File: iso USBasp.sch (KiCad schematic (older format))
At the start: 103 parts

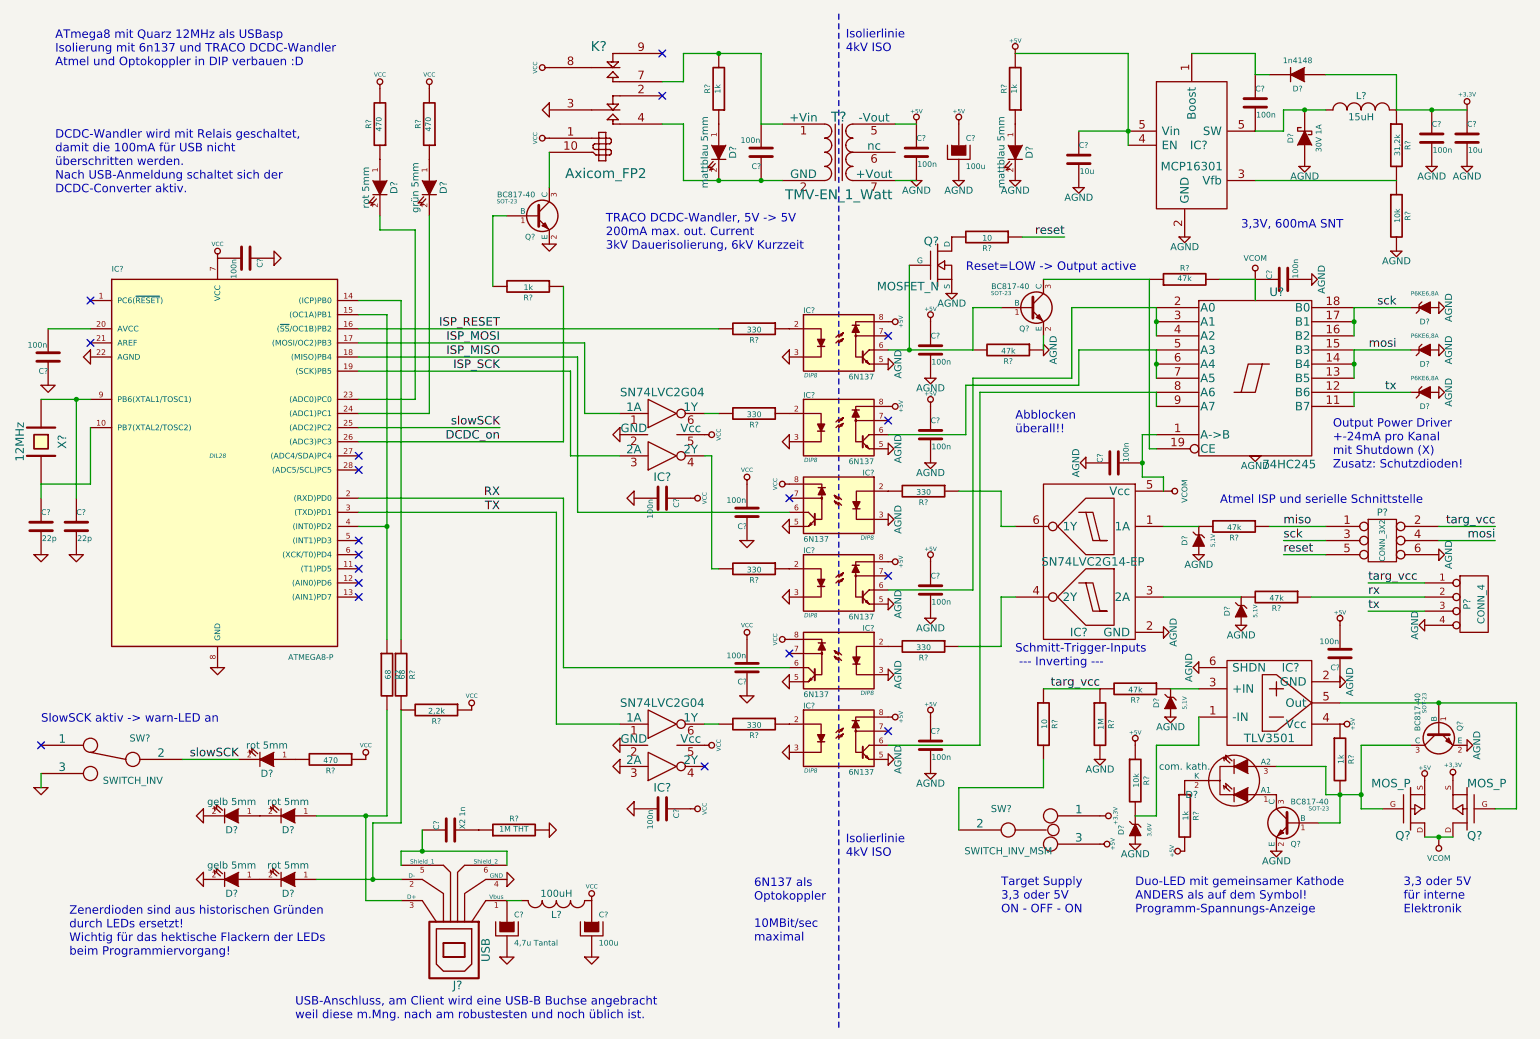
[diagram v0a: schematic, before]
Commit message: zuordunugsdateien schaltplan -> footprints dazu, aber noch nicht fertig. + noch ein paar Änderungen am Schaltplan
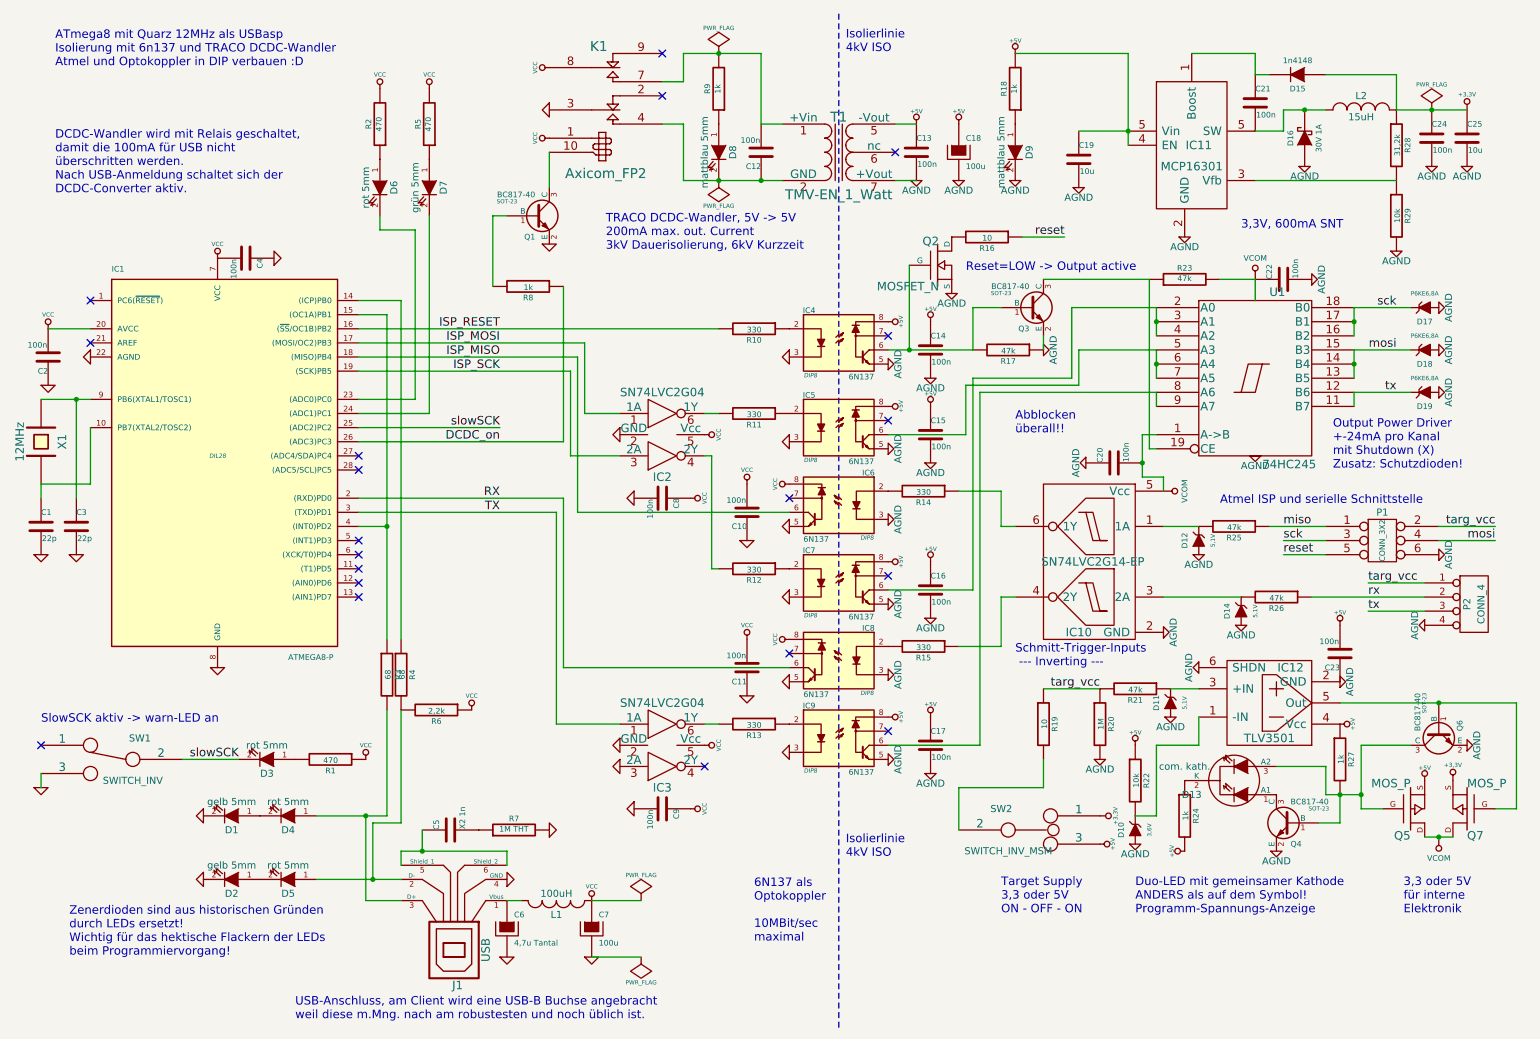
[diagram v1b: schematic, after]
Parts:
- gave numbers to parts that had none: 103
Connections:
- net VCC: now also C2.2, IC1.20 (AVCC)
- no-connect marks 19 -> 20

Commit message: neue Footprints für MOSFETs und Schalter dazugefügt.
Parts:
- Q5, Q7: value MOS_P -> IRF7410
- SW1: value SWITCH_INV -> APEM SS25136NH
- SW2: value SWITCH_INV_MSM -> APEM SS25139NH
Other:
- note added: "Zenerdioden sind aus historischen Gründen\ndurch 5mm-Standard-LEDs ersetzt!\nWichtig für das hektische Flackern der LEDs\nbeim Programmiervorgang!"
- note removed: "Zenerdioden sind aus historischen Gründen\ndurch LEDs ersetzt!\nWichtig für das hektische Flackern der LEDs\nbeim Programmiervorgang!"
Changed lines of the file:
@@
 Connection ~ 3000 6200
 Text Notes 900  7200 0    60   ~ 0
-Zenerdioden sind aus historischen Gründen\ndurch LEDs ersetzt!\nWichtig für das hektische Flackern der LEDs\nbeim Programmiervorgang!
+Zenerdioden sind aus historischen Gründen\ndurch 5mm-Standard-LEDs ersetzt!\nWichtig für das hektische Flackern der LEDs\nbeim Programmiervorgang!
 NoConn ~ 1050 2550
 Wire Wire Line
@@
 P 7700 6300
 F 0 "SW2" H 7501 6450 50  0000 C CNN
-F 1 "SWITCH_INV_MSM" H 7551 6151 50  0000 C CNN
+F 1 "APEM SS25139NH" H 7551 6151 50  0000 C CNN
 F 2 "" H 7700 6300 60  0000 C CNN
 F 3 "" H 7700 6300 60  0000 C CNN
@@
 P 10800 6150
 F 0 "Q7" H 10800 6340 60  0000 R CNN
-F 1 "MOS_P" H 10800 5970 60  0000 R CNN
+F 1 "IRF7410" H 10800 5970 60  0000 R CNN
 F 2 "" H 10800 6150 60  0000 C CNN
 F 3 "" H 10800 6150 60  0000 C CNN
@@
 P 10400 6150
 F 0 "Q5" H 10400 6340 60  0000 R CNN
-F 1 "MOS_P" H 10400 5970 60  0000 R CNN
+F 1 "IRF7410" H 10400 5970 60  0000 R CNN
 F 2 "" H 10400 6150 60  0000 C CNN
 F 3 "" H 10400 6150 60  0000 C CNN
@@
 P 1200 5800
 F 0 "SW1" H 1000 5950 50  0000 C CNN
-F 1 "SWITCH_INV" H 1050 5650 50  0000 C CNN
+F 1 "APEM SS25136NH" H 1050 5650 50  0000 C CNN
 F 2 "" H 1200 5800 60  0000 C CNN
 F 3 "" H 1200 5800 60  0000 C CNN

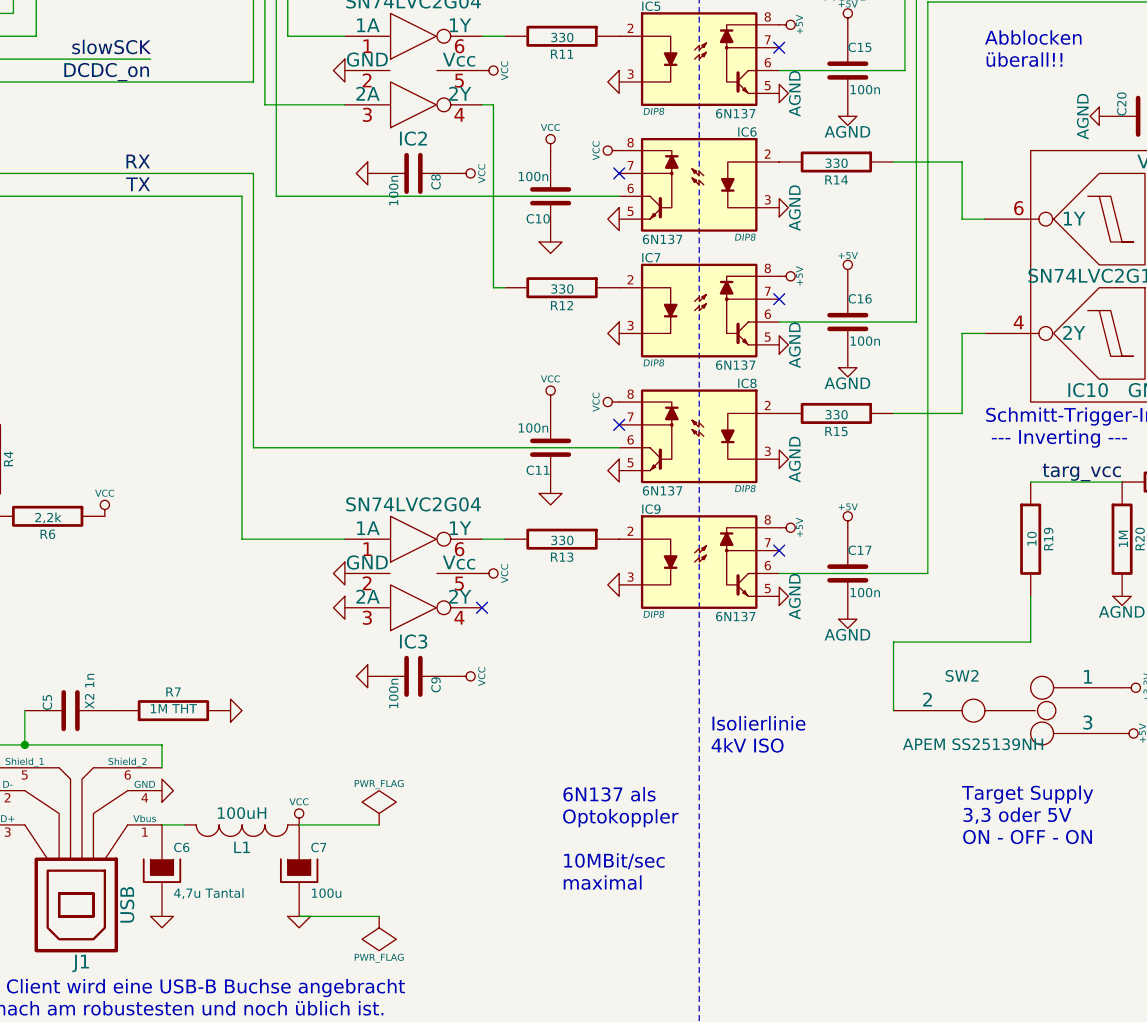
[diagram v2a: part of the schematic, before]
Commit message: Anfang des Layouts, der USB-verbundene Teil ist schon fast fertig. es fehlen noch die Footprints von Schaltern und dem TRACO-DCDC-Wandler
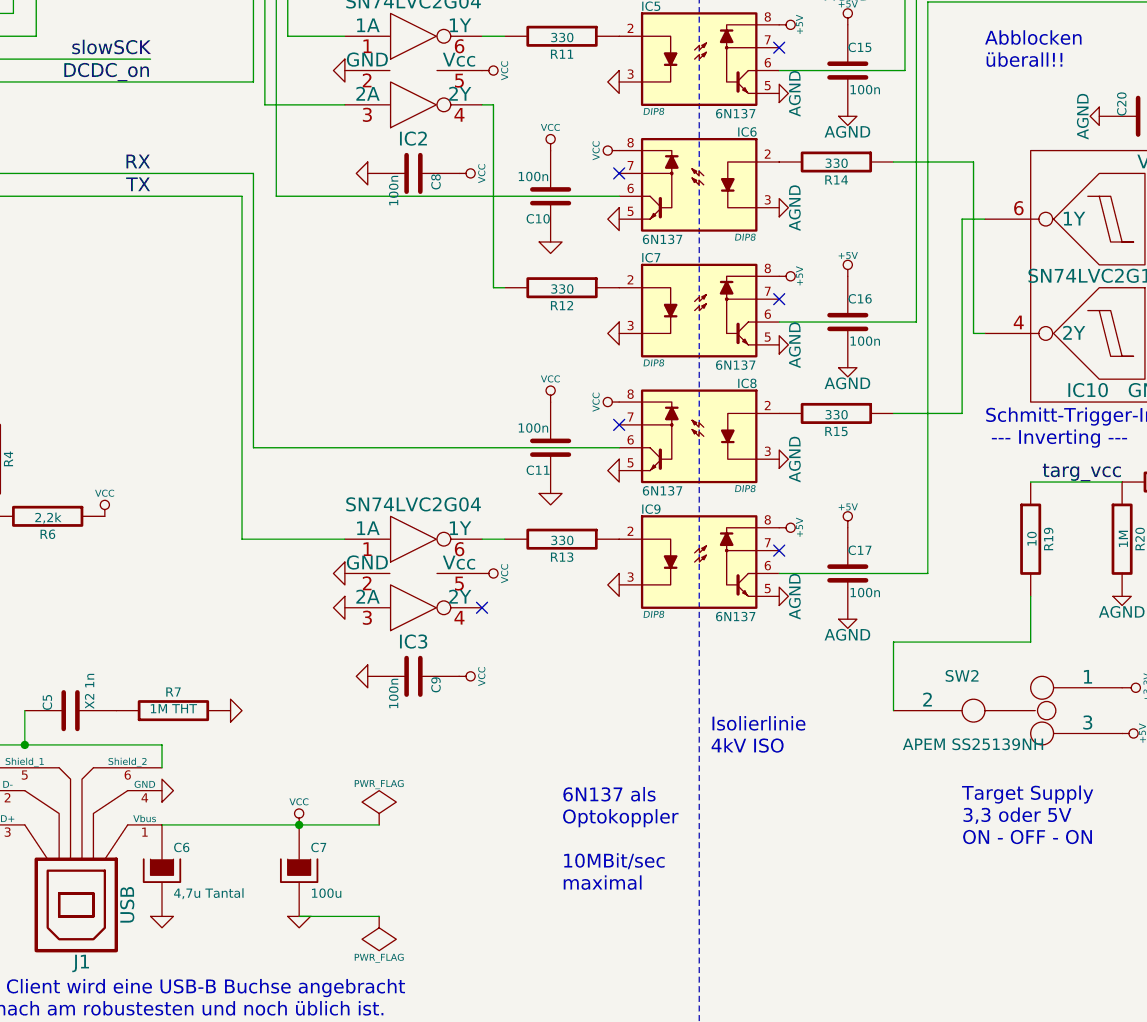
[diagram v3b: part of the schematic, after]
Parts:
- removed L1: 100uH, symbol INDUCTOR_SMALL
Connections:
- net VCC: now also C6.1, J1.1 (Vbus)
- net at R14.1: now also IC10.4 (2Y); no longer IC10.6 (1Y)
- net at R15.1: now also IC10.6 (1Y); no longer IC10.4 (2Y)
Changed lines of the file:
@@
 	1    0    0    -1
 $EndComp
-$Comp
-L INDUCTOR_SMALL L1
-U 1 1 531B8EE3
-P 4350 6800
-F 0 "L1" H 4350 6900 50  0000 C CNN
-F 1 "100uH" H 4350 6750 50  0000 C CNN
-F 2 "" H 4350 6800 60  0000 C CNN
-F 3 "" H 4350 6800 60  0000 C CNN
-	1    4350 6800
-	-1   0    0    1
-$EndComp
-Wire Wire Line
-	4100 6800 4000 6800
-Wire Wire Line
-	4600 6800 4950 6800
+Wire Wire Line
+	4000 6800 4950 6800
 Wire Wire Line
 	3350 3250 3350 2050
@@
 Output Power Driver\n+-24mA pro Kanal\nmit Shutdown (X)\nZusatz: Schutzdioden!
 Wire Wire Line
-	7200 3900 7500 3900
-Wire Wire Line
-	7200 5000 7500 5000
+	7200 3900 7550 3900
+Wire Wire Line
+	7500 5000 7200 5000
 $Comp
 L AGND #PWR066
@@
 Text Notes 7600 5150 0    60   ~ 0
 Schmitt-Trigger-Inputs\n --- Inverting ---
-Wire Wire Line
-	7500 5000 7500 4650
-Wire Wire Line
-	7500 4650 7600 4650
-Wire Wire Line
-	7600 4150 7500 4150
-Wire Wire Line
-	7500 4150 7500 3900
 Text Notes 4700 2200 0    60   ~ 0
 TRACO DCDC-Wandler, 5V -> 5V\n200mA max. out. Current\n3kV Dauerisolierung, 6kV Kurzzeit
@@
 	-1   0    0    1
 $EndComp
+Connection ~ 4600 6800
+Wire Wire Line
+	7500 4150 7600 4150
+Wire Wire Line
+	7550 3900 7550 4650
+Wire Wire Line
+	7550 4650 7600 4650
+Wire Wire Line
+	7500 5000 7500 4150
 $EndSCHEMATC
